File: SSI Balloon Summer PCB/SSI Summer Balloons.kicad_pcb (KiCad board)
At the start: 2 copper layers, 107 parts, among them J1 Battery connector, J3 LoRa antenna, J4 APRS antenna, J5 Conn_01x05, J7 GPS antenna, J8 PT1000 Sensor, J9 Camera, Q2 DMG2305UX-7, SW1 412k, SW2 SW_SPST, SW3 SW_SPST, U1 RFM95W-915S2, U10 MS5611-01BA03, U11 TPS63070RNMR, U12 TPS63070RNMR, U3 AP2112K-3.3TRG1, U4 ICM-42688-P, U5 DRA818V, U7 STM32F411CEUx, U8 MAX-M10S-00B, U9 MAX31865ATP_T, Y1 ABM8W-12.0000MHZ-8-K1Z-T3

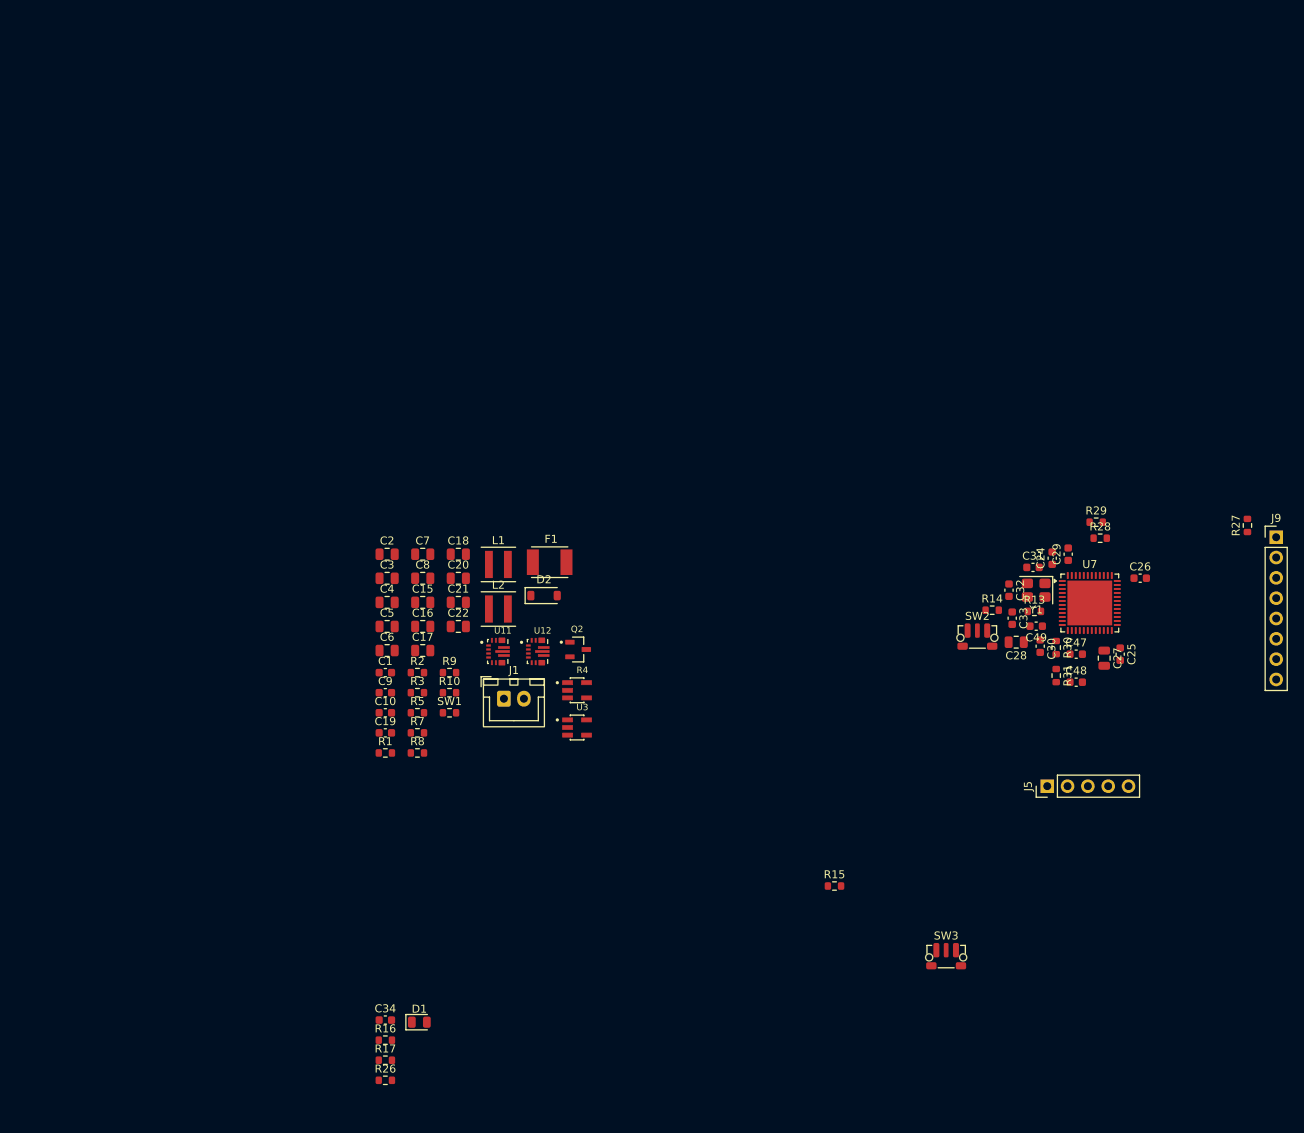
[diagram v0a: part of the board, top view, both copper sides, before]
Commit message: finished SD card placement - only Power sheet left
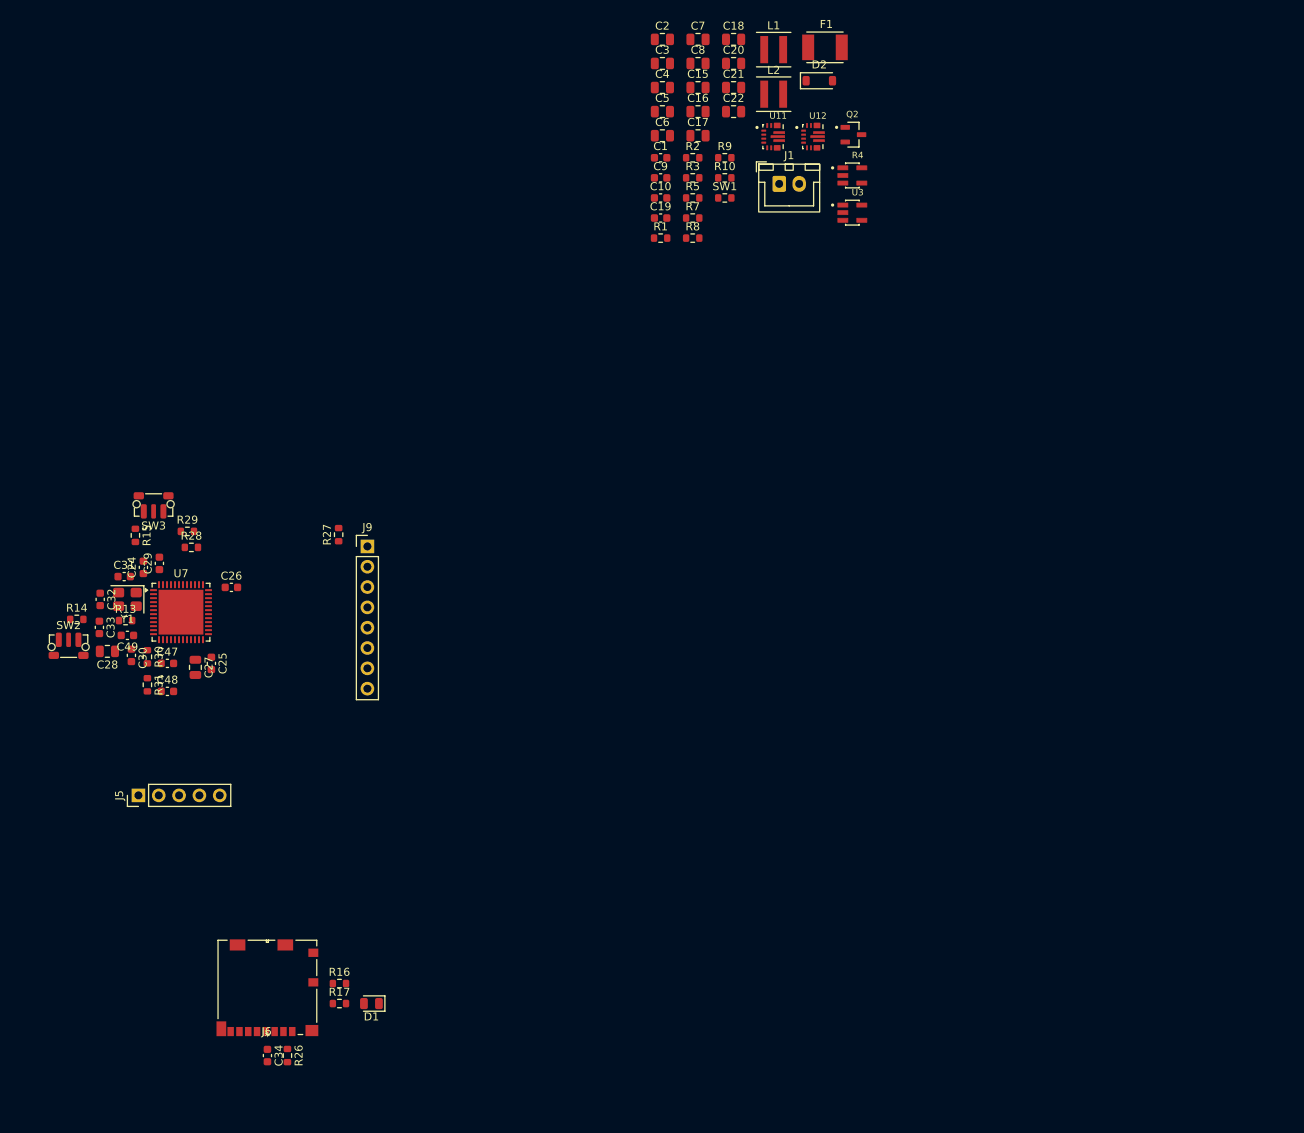
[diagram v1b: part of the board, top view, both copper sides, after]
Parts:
- added J6: 1040310811, 1040310811:104031-0811_MOL, F.Cu at (133.4, 147.7)
- moved R14 114.4 mm to (109.6, 101.7)
- moved SW3 114.1 mm to (119.2, 87.2), turned to 180 degrees
- moved C33 114.1 mm to (112.4, 102.7)
- moved R13 113.6 mm to (115.7, 101.8)
- moved SW2 113.6 mm to (108.5, 105.1)
- moved C24 113.6 mm to (117.9, 95.2)
- moved C25 113.6 mm to (126.4, 107.2)
- moved C26 113.6 mm to (128.9, 97.7)
- moved C27 113.6 mm to (124.4, 107.7)
- moved C28 113.6 mm to (113.4, 105.7)
- moved C29 113.6 mm to (119.9, 94.7)
- moved C30 113.6 mm to (116.4, 106.2)
- moved C31 113.6 mm to (115.5, 96.3)
- moved C32 113.6 mm to (112.5, 99.2)
- moved C47 113.6 mm to (120.9, 107.2)
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
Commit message: Reviewed sensor sheet
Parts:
- removed R16: 10k, Resistor_SMD:R_0603_1608Metric
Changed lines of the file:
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@@
-		)
-	)
-	(footprint "Resistor_SMD:R_0603_1608Metric"
-		(layer "F.Cu")
-		(at 142.405 147.1715)
-		(descr "Resistor SMD 0603 (1608 Metric), square (rectangular) end terminal, IPC-7351 nominal, (Body size source: IPC-SM-782 page 72, https://www.pcb-3d.com/wordpress/wp-content/uploads/ipc-sm-782a_amendment_1_and_2.pdf)")
-		(tags "resistor")
-		(property "Reference" "R16"
-			(at 0 -1.43 0)
-			(layer "F.SilkS")
-			(effects
-				(font
-					(size 1 1)
-					(thickness 0.15)
-				)
-			)
-		)
-		(property "Value" "10k"
-			(at 0 1.43 0)
-			(layer "F.Fab")
-			(effects
-				(font
-					(size 1 1)
-					(thickness 0.15)
-				)
-			)
-		)
-		(property "Datasheet" ""
-			(at 0 0 0)
-			(layer "F.Fab")
-			(hide yes)
-			(effects
-				(font
-					(size 1.27 1.27)
-				)
-			)
-		)
-		(property "Description" "Resistor"
-			(at 0 0 0)
-			(layer "F.Fab")
-			(hide yes)
-			(effects
-				(font
-					(size 1.27 1.27)
-				)
-			)
-		)
-		(property "KiLib_Generator" "SMD_2terminal_chip_molded"
-			(at 0 0 0)
-			(layer "F.SilkS")
-			(hide yes)
-			(effects
-				(font
-					(size 1 1)
-					(thickness 0.15)
-				)
-			)
-		)
-		(property ki_fp_filters "R_*")
-		(sheetname "/microSD/")
-		(sheetfile "microSD.kicad_sch")
-		(units
-			(unit
-				(name "A")
-				(pins "1" "2")
-			)
-		)
-		(attr smd)
-		(duplicate_pad_numbers_are_jumpers no)
-		(fp_line
-			(start -0.237258 -0.5225)
-			(end 0.237258 -0.5225)
-			(stroke
-				(width 0.12)
-				(type solid)
-			)
-			(layer "F.SilkS")
-		)
-		(fp_line
-			(start -0.237258 0.5225)
-			(end 0.237258 0.5225)
-			(stroke
-				(width 0.12)
-				(type solid)
-			)
-			(layer "F.SilkS")
-		)
-		(fp_rect
-			(start -1.48 -0.73)
-			(end 1.48 0.73)
-			(stroke
-				(width 0.05)
-				(type solid)
-			)
-			(fill no)
-			(layer "F.CrtYd")
-		)
-		(fp_rect
-			(start -0.8 -0.4125)
-			(end 0.8 0.4125)
-			(stroke
-				(width 0.1)
-				(type solid)
-			)
-			(fill no)
-			(layer "F.Fab")
-		)
-		(fp_text user "${REFERENCE}"
-			(at 0 0 0)
-			(layer "F.Fab")
-			(effects
-				(font
-					(size 0.4 0.4)
-					(thickness 0.06)
-				)
-			)
-		)
-		(pad "1" smd roundrect
-			(at -0.825 0)
-			(size 0.8 0.95)
-			(layers "F.Cu" "F.Mask" "F.Paste")
-			(roundrect_rratio 0.25)
-			(net "/MCU (STM)/microSD_detect")
-			(pintype "passive")
-		)
-		(pad "2" smd roundrect
-			(at 0.825 0)
-			(size 0.8 0.95)
-			(layers "F.Cu" "F.Mask" "F.Paste")
-			(roundrect_rratio 0.25)
-			(net "GND")
-			(pintype "passive")
-		)
-		(embedded_fonts no)
-		(model "${KICAD10_3DMODEL_DIR}/Resistor_SMD.3dshapes/R_0603_1608Metric.step"
-			(offset
-				(xyz 0 0 0)
-			)
-			(scale
-				(xyz 1 1 1)
-			)
-			(rotate
-				(xyz 0 0 0)
-			)
 		)
 	)

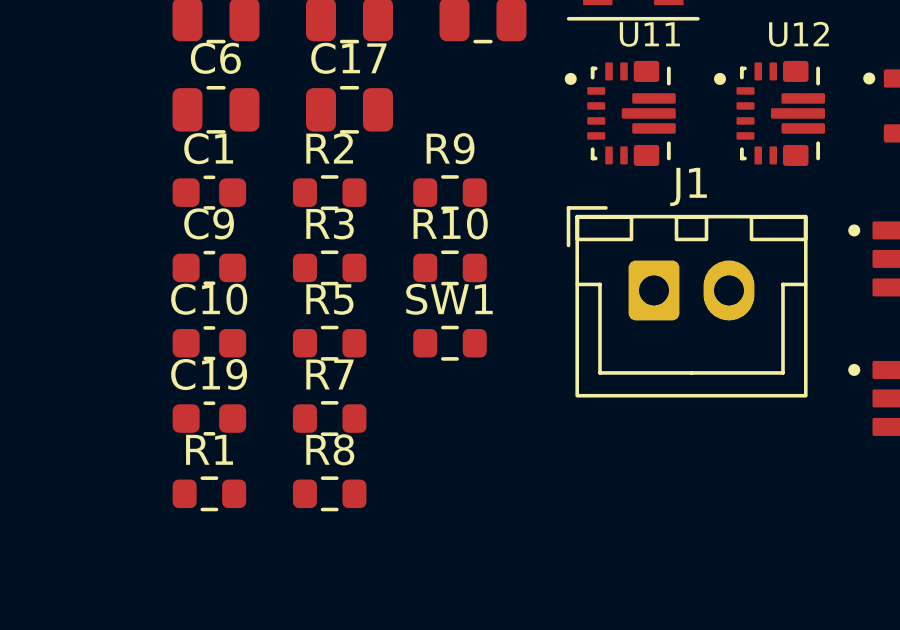
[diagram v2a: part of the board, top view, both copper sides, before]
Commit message: Reviewed Radio, GPS sheet and minor tweak on power sheet
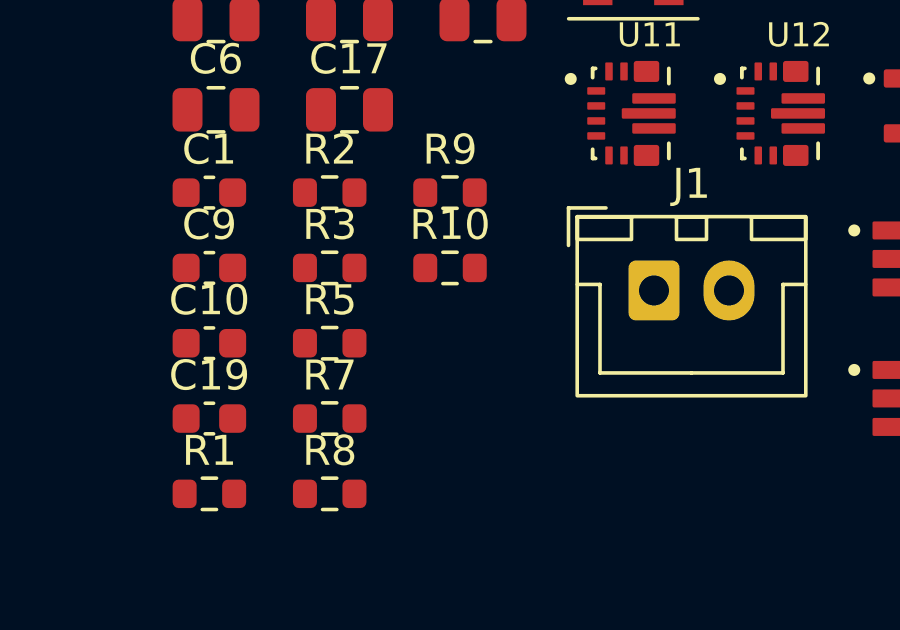
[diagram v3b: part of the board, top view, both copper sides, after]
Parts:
- removed SW1: 412k, Resistor_SMD:R_0603_1608Metric
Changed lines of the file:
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@@
-		)
-	)
-	(footprint "Resistor_SMD:R_0603_1608Metric"
-		(layer "F.Cu")
-		(at 190.575 48.97)
-		(descr "Resistor SMD 0603 (1608 Metric), square (rectangular) end terminal, IPC-7351 nominal, (Body size source: IPC-SM-782 page 72, https://www.pcb-3d.com/wordpress/wp-content/uploads/ipc-sm-782a_amendment_1_and_2.pdf)")
-		(tags "resistor")
-		(property "Reference" "SW1"
-			(at 0 -1.43 0)
-			(layer "F.SilkS")
-			(effects
-				(font
-					(size 1 1)
-					(thickness 0.15)
-				)
-			)
-		)
-		(property "Value" "412k"
-			(at 0 1.43 0)
-			(layer "F.Fab")
-			(effects
-				(font
-					(size 1 1)
-					(thickness 0.15)
-				)
-			)
-		)
-		(property "Datasheet" ""
-			(at 0 0 0)
-			(layer "F.Fab")
-			(hide yes)
-			(effects
-				(font
-					(size 1.27 1.27)
-				)
-			)
-		)
-		(property "Description" "Resistor"
-			(at 0 0 0)
-			(layer "F.Fab")
-			(hide yes)
-			(effects
-				(font
-					(size 1.27 1.27)
-				)
-			)
-		)
-		(property "KiLib_Generator" "SMD_2terminal_chip_molded"
-			(at 0 0 0)
-			(layer "F.SilkS")
-			(hide yes)
-			(effects
-				(font
-					(size 1 1)
-					(thickness 0.15)
-				)
-			)
-		)
-		(sheetname "/Power/")
-		(sheetfile "Power.kicad_sch")
-		(units
-			(unit
-				(name "A")
-				(pins "2" "1" "3")
-			)
-		)
-		(attr smd)
-		(duplicate_pad_numbers_are_jumpers no)
-		(fp_line
-			(start -0.237258 -0.5225)
-			(end 0.237258 -0.5225)
-			(stroke
-				(width 0.12)
-				(type solid)
-			)
-			(layer "F.SilkS")
-		)
-		(fp_line
-			(start -0.237258 0.5225)
-			(end 0.237258 0.5225)
-			(stroke
-				(width 0.12)
-				(type solid)
-			)
-			(layer "F.SilkS")
-		)
-		(fp_rect
-			(start -1.48 -0.73)
-			(end 1.48 0.73)
-			(stroke
-				(width 0.05)
-				(type solid)
-			)
-			(fill no)
-			(layer "F.CrtYd")
-		)
-		(fp_rect
-			(start -0.8 -0.4125)
-			(end 0.8 0.4125)
-			(stroke
-				(width 0.1)
-				(type solid)
-			)
-			(fill no)
-			(layer "F.Fab")
-		)
-		(fp_text user "${REFERENCE}"
-			(at 0 0 0)
-			(layer "F.Fab")
-			(effects
-				(font
-					(size 0.4 0.4)
-					(thickness 0.06)
-				)
-			)
-		)
-		(pad "1" smd roundrect
-			(at -0.825 0)
-			(size 0.8 0.95)
-			(layers "F.Cu" "F.Mask" "F.Paste")
-			(roundrect_rratio 0.25)
-			(net "Net-(SW1-A)")
-			(pinfunction "A_1")
-			(pintype "passive")
-		)
-		(pad "2" smd roundrect
-			(at 0.825 0)
-			(size 0.8 0.95)
-			(layers "F.Cu" "F.Mask" "F.Paste")
-			(roundrect_rratio 0.25)
-			(net "VBAT")
-			(pinfunction "B_2")
-			(pintype "passive")
-		)
-		(embedded_fonts no)
-		(model "${KICAD10_3DMODEL_DIR}/Resistor_SMD.3dshapes/R_0603_1608Metric.step"
-			(offset
-				(xyz 0 0 0)
-			)
-			(scale
-				(xyz 1 1 1)
-			)
-			(rotate
-				(xyz 0 0 0)
-			)
 		)
 	)

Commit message: layout board layers + rules
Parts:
- removed R3, R8: 100k, Resistor_SMD:R_0603_1608Metric
- added J2: Conn_01x02, Connector_JST:JST_PH_B2B-PH-K_1x02_P2.00mm_Vertical, F.Cu at (14.1, -35.3)
- C17, C18, C5, C6: footprint Capacitor_SMD:C_0805_2012Metric -> Capacitor_SMD:C_0603_1608Metric
- moved J1 214.0 mm to (0.17, -35.8), turned to 90 degrees
- moved Q2 193.1 mm to (30.2, -37.3), turned to 180 degrees
- moved F1 192.2 mm to (23.2, -37.3)
- moved D2 181.5 mm to (35.2, -36.3), turned to -90 degrees
- moved R1 172.4 mm to (32.2, -30.3), turned to 90 degrees
- moved R4 122.8 mm to (107.5, 118.8), turned to 180 degrees
- moved L1 115.4 mm to (116.0, 113.0), turned to -90 degrees
- moved U11 111.8 mm to (110.8, 113.0)
- moved C3 109.9 mm to (114.5, 118.3), turned to 90 degrees
- moved C8 109.5 mm to (109.5, 109.3)
- moved C2 109.3 mm to (117.5, 116.8), turned to 180 degrees
- moved C4 109.2 mm to (112.0, 118.3), turned to 90 degrees
- moved C7 107.9 mm to (114.5, 108.8), turned to -90 degrees
- moved C5 107.5 mm to (110.0, 117.3), turned to 90 degrees
- moved U3 106.4 mm to (124.8, 119.0)
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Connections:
- U11 pad 2: Net-(U11-PG) -> unconnected-(U11-PG-Pad2)
- U12 pad 2: Net-(U12-PG) -> unconnected-(U12-PG-Pad2)
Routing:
- added copper zone on In1.Cu, net GND
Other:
- board outline added: 80 x 59 mm
- copper layers 2 -> 4

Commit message: Removed sketchy R4 footprint
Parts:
- removed R4: 680k, AP2112K-3.3TRG1:SOT95P285X140-5N
- added R3: 680k, Resistor_SMD:R_0603_1608Metric, F.Cu at (107.0, 119.0)
- added R3: 680k, Resistor_SMD:R_0201_0603Metric, F.Cu at (0.72, 0.38)
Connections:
- net /MCU (STM)/+5V renamed +5V
- net /Power/+4V1 renamed +4V1
- net /Power/VBAT_PROT renamed VBAT_PROT
- C43 pad 1: GND -> +3V3
- C43 pad 2: +3V3 -> GND
- F1 pad 1: Net-(J2-Pin_2) -> Net-(SW1-A)
- R25 pad 1: +3V3 -> /MCU (STM)/BARO_CS
- R25 pad 2: /MCU (STM)/BARO_CS -> +3V3
- R28 pad 1: /MCU (STM)/SCL -> +3V3
- R28 pad 2: +3V3 -> /MCU (STM)/SCL
- R29 pad 1: /MCU (STM)/SDA -> +3V3
- R29 pad 2: +3V3 -> /MCU (STM)/SDA
